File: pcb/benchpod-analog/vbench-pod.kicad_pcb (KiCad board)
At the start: 4 copper layers, 98.9 x 118.2 mm, 236 parts, among them CN1 KH-FPC1.0-H2.0SMT-24P-QCHF, J10 BNC-KYWE-295-W4-N, J11 WJ15EDGRC-3.81-06P, J8 WJ15EDGRC-3.81-02P, J9 WJ15EDGRC-3.81-02P, K1 G6K-2F-Y DC5, K2 G6K-2F-Y DC5, K3 G6K-2F-Y DC5, K4 G6K-2F-Y DC5, Q1 BCP56, U15 TPS7A2045PDBVR, U16 TLV61046ADBVR, U17 TMCP1A106MTRF, U3 TPS7A2050PDQNR, U30 AP2112K-3.3, U36 MCP33131D-10-E/MS, U37 THS4551IRUNR, U38 ADR4540BRZ-R7, U39 AP2112K-1.8TRG1, U40 OPA810IDBVR, U41 LM27761DSGR, U42 LM7705MM/NOPB, U43 DAC8554IPWR, U44 OPA2365AIDR, U45 OPA2992IDR, U46 AP2112K-3.3, U49 TPS65131RGER, U50 TPS7A1901DRBR, U51 OPA2992IDR, U53 TPL7407LAPWR, U58 TCA9554PWR, U61 24C32, U9 XTR116UA/2K5

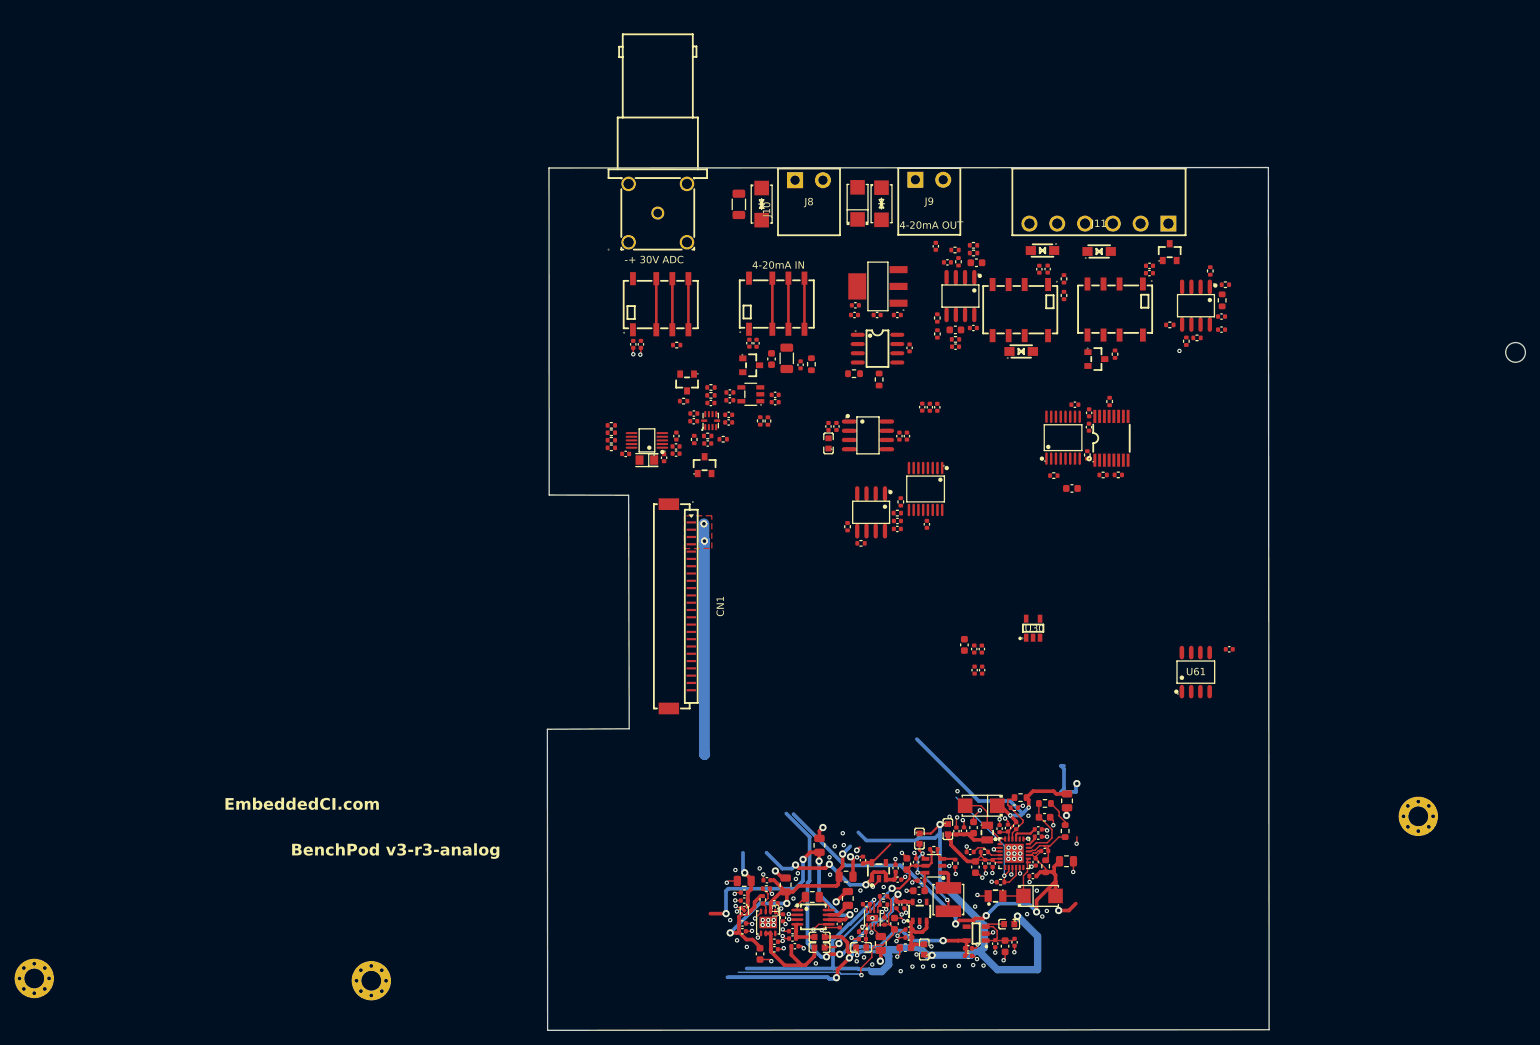
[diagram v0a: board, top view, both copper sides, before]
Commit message: analog only board: square outline, front connectors overhang, J8/J9 turned
Parts moved only; tracks are not rerouted.
- Outline: one polygon, exactly 98.5 x 118 (x 39.0-137.5, y 20.18-138.18),
  with the FFC cut (x to 50.0, y 65.0-97.0) and a 2.2 mm tab under the BNC
  (x 46.41-61.41) so its pads stay on the board while it reaches the panel.
- J10 (ADC BNC): flange front on the panel's inside face (2.4 mm past the
  edge), so the panel nut clamps it; y 26.36 -> 23.78.
- J8 (4-20 IN), J9 (4-20 OUT): were at 0 deg, with the plug opening facing
  into the board; now 180 deg like J11, opening 2.2 mm past the edge.
- J11 (DAC block): 2.2 mm overhang, x 114.37 -> 115.22 for the same
  7.89 mm gap as between J8 and J9.
- J8, J9 and J10 keep their x; nothing else moved.

Co-Authored-By: Claude Opus 5.5 <noreply@anthropic.com>
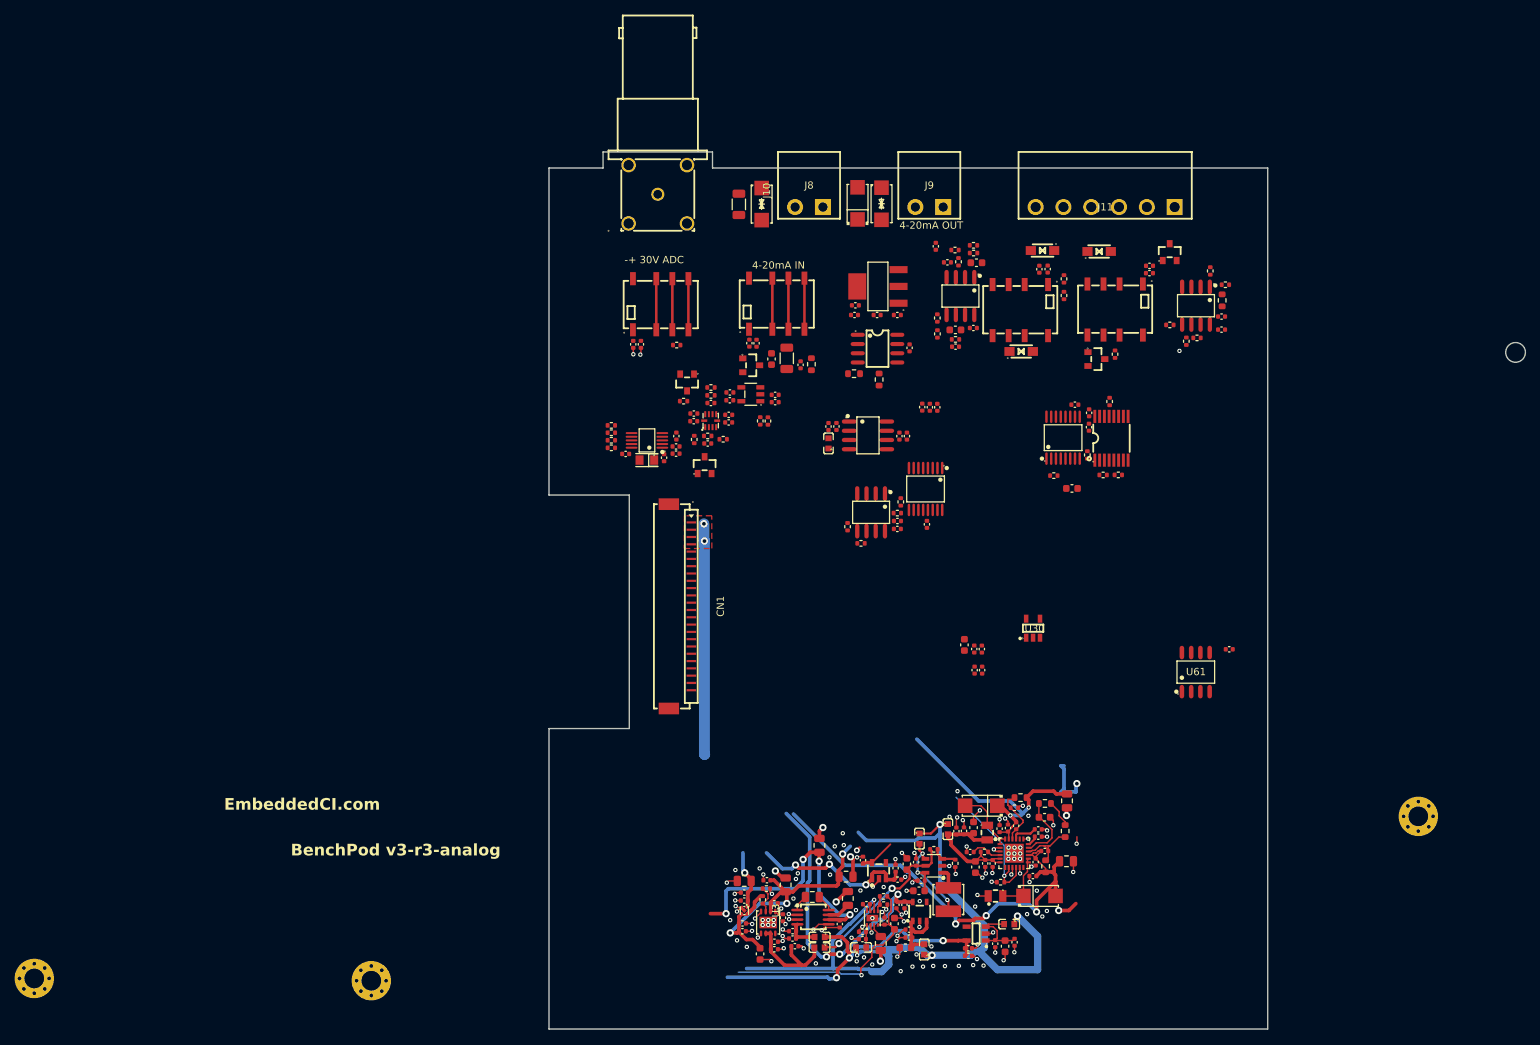
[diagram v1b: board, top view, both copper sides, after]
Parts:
- moved J9 3.74 mm to (91.1, 25.5), turned to 180 degrees
- moved J8 3.68 mm to (74.6, 25.5), turned to 180 degrees
- moved J10 2.58 mm to (53.9, 23.8)
- moved J11 2.42 mm to (115.2, 25.5)
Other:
- board size 98.9 x 118.2 mm -> 98.5 x 120.2 mm

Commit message: analog only board: mounting holes at the digital board's positions
H10, H11, H12, H14 at the same X/Y from the top-left board corner as on the
digital board (x 5.99 / 92.33, y 20.81 / 92.49), so both boards line up
in the case. H10, H11 and H14 sit in free space. H12 lands on U45
(OPA2992), C168, C169 and R108: those need to move. H12 is still the
unplated MountingHole_2.7mm_M2.5 here (plated Pad_Via on the digital
board).

Co-Authored-By: Claude Opus 5.5 <noreply@anthropic.com>
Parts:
- moved H10 95.5 mm to (45.0, 41.0), turned to 0 degrees
- moved H11 78.8 mm to (45.0, 112.7), turned to 0 degrees
- moved H12 40.4 mm to (131.3, 41.0)
- moved H14 27.1 mm to (131.3, 112.7)
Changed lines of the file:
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@@
 	(footprint "MountingHole:MountingHole_2.7mm_M2.5_Pad_Via"
 		(layer "F.Cu")
-		(at 14.65 131.558218 -90)
+		(at 44.992 40.986)
 		(descr "Mounting Hole 2.7mm, M2.5, generated by kicad-footprint-generator mountinghole.py")
 		(tags "mountinghole M2.5")
 		(property "Reference" "H10"
-			(at 0 -3.65 90)
+			(at 0 -3.65 180)
 			(layer "F.SilkS")
 			(hide yes)
@@
 		)
 		(property "Value" "MountingHole"
-			(at 0 3.65 90)
+			(at 0 3.65 180)
 			(layer "F.Fab")
 			(effects
@@
 		)
 		(property "Datasheet" ""
-			(at 0 0 90)
+			(at 0 0 180)
 			(layer "F.Fab")
 			(hide yes)
@@
 		)
 		(property "Description" "Mounting Hole with connection"
-			(at 0 0 90)
+			(at 0 0 180)
 			(layer "F.Fab")
 			(hide yes)
@@
 		)
 		(pad "1" thru_hole circle
-			(at -2.025 0 270)
+			(at -2.025 0)
 			(size 0.8 0.8)
 			(drill 0.5)
@@
 		)
 		(pad "1" thru_hole circle
-			(at -1.431891 -1.431891 270)
+			(at -1.431891 -1.431891)
 			(size 0.8 0.8)
 			(drill 0.5)
@@
 		)
 		(pad "1" thru_hole circle
-			(at -1.431891 1.431891 270)
+			(at -1.431891 1.431891)
 			(size 0.8 0.8)
 			(drill 0.5)
@@
 		)
 		(pad "1" thru_hole circle
-			(at 0 -2.025 270)
+			(at 0 -2.025)
 			(size 0.8 0.8)
 			(drill 0.5)
@@
 		)
 		(pad "1" thru_hole circle
-			(at 0 0 270)
+			(at 0 0)
 			(size 5.4 5.4)
 			(drill 2.7)
@@
 		)
 		(pad "1" thru_hole circle
-			(at 0 2.025 270)
+			(at 0 2.025)
 			(size 0.8 0.8)
 			(drill 0.5)
@@
 		)
 		(pad "1" thru_hole circle
-			(at 1.431891 -1.431891 270)
+			(at 1.431891 -1.431891)
 			(size 0.8 0.8)
 			(drill 0.5)
@@
 		)
 		(pad "1" thru_hole circle
-			(at 1.431891 1.431891 270)
+			(at 1.431891 1.431891)
 			(size 0.8 0.8)
 			(drill 0.5)
@@
 		)
 		(pad "1" thru_hole circle
-			(at 2.025 0 270)
+			(at 2.025 0)
 			(size 0.8 0.8)
 			(drill 0.5)
@@
 	(footprint "MountingHole:MountingHole_2.7mm_M2.5_Pad_Via"
 		(layer "F.Cu")
-		(at -31.538109 131.251109 -90)
+		(at 44.992 112.67)
 		(descr "Mounting Hole 2.7mm, M2.5, generated by kicad-footprint-generator mountinghole.py")
 		(tags "mountinghole M2.5")
 		(property "Reference" "H11"
-			(at 0 -3.65 90)
+			(at 0 -3.65 180)
 			(layer "F.SilkS")
 			(hide yes)
@@
 		)
 		(property "Value" "MountingHole"
-			(at 0 3.65 90)
+			(at 0 3.65 180)
 			(layer "F.Fab")
 			(effects
@@
 		)
 		(property "Datasheet" ""
-			(at 0 0 90)
+			(at 0 0 180)
 			(layer "F.Fab")
 			(hide yes)
@@
 		)
 		(property "Description" "Mounting Hole with connection"
-			(at 0 0 90)
+			(at 0 0 180)
 			(layer "F.Fab")
 			(hide yes)
@@
 		)
 		(pad "1" thru_hole circle
-			(at -2.025 0 270)
+			(at -2.025 0)
 			(size 0.8 0.8)
 			(drill 0.5)
@@
 		)
 		(pad "1" thru_hole circle
-			(at -1.431891 -1.431891 270)
+			(at -1.431891 -1.431891)
 			(size 0.8 0.8)
 			(drill 0.5)
@@
 		)
 		(pad "1" thru_hole circle
-			(at -1.431891 1.431891 270)
+			(at -1.431891 1.431891)
 			(size 0.8 0.8)
 			(drill 0.5)
@@
 		)
 		(pad "1" thru_hole circle
-			(at 0 -2.025 270)
+			(at 0 -2.025)
 			(size 0.8 0.8)
 			(drill 0.5)
@@
 		)
 		(pad "1" thru_hole circle
-			(at 0 0 270)
+			(at 0 0)
 			(size 5.4 5.4)
 			(drill 2.7)
@@
 		)
 		(pad "1" thru_hole circle
-			(at 0 2.025 270)
+			(at 0 2.025)
 			(size 0.8 0.8)
 			(drill 0.5)
@@
 		)
 		(pad "1" thru_hole circle
-			(at 1.431891 -1.431891 270)
+			(at 1.431891 -1.431891)
 			(size 0.8 0.8)
 			(drill 0.5)
@@
 		)
 		(pad "1" thru_hole circle
-			(at 1.431891 1.431891 270)
+			(at 1.431891 1.431891)
 			(size 0.8 0.8)
 			(drill 0.5)
@@
 		)
 		(pad "1" thru_hole circle
-			(at 2.025 0 270)
+			(at 2.025 0)
 			(size 0.8 0.8)
 			(drill 0.5)
@@
 	(footprint "MountingHole:MountingHole_2.7mm_M2.5_Pad_Via"
 		(layer "F.Cu")
-		(at 158.138 109.034)
+		(at 131.332999 112.67)
 		(descr "Mounting Hole 2.7mm, M2.5, generated by kicad-footprint-generator mountinghole.py")
 		(tags "mountinghole M2.5")
@@
 	(footprint "MountingHole:MountingHole_2.7mm_M2.5"
 		(layer "F.Cu")
-		(at 171.463 45.452)
+		(at 131.332999 40.986)
 		(descr "Mounting Hole 2.7mm, M2.5, no annular, generated by kicad-footprint-generator mountinghole.py")
 		(tags "mountinghole M2.5")

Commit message: analog only board: H12 plated and on GND like the other holes
H12 becomes Mechanical:MountingHole_Pad with MountingHole_2.7mm_M2.5_Pad_Via
and its own GND symbol, the same as H10, H11, H14 and all four holes on the
digital board. PCB footprint swapped in place (same position, path, GND on
the pads). Its pad now shorts with U45, C168, C169 and R108, which still
need to move out of the hole's keepout.

Co-Authored-By: Claude Opus 5.5 <noreply@anthropic.com>
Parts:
- H12: footprint MountingHole:MountingHole_2.7mm_M2.5 -> MountingHole:MountingHole_2.7mm_M2.5_Pad_Via
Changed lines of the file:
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@@
 		)
 	)
+	(footprint "MountingHole:MountingHole_2.7mm_M2.5_Pad_Via"
+		(layer "F.Cu")
+		(at 131.332999 40.986)
+		(descr "Mounting Hole 2.7mm, M2.5, generated by kicad-footprint-generator mountinghole.py")
+		(tags "mountinghole M2.5")
+		(property "Reference" "H12"
+			(at 0 -3.65 0)
+			(layer "F.SilkS")
+			(effects
+				(font
+					(size 1 1)
+					(thickness 0.15)
+				)
+			)
+		)
+		(property "Value" "MountingHole"
+			(at 0 3.65 0)
+			(layer "F.Fab")
+			(effects
+				(font
+					(size 1 1)
+					(thickness 0.15)
+				)
+			)
+		)
+		(property "Datasheet" ""
+			(at 0 0 0)
+			(layer "F.Fab")
+			(hide yes)
+			(effects
+				(font
+					(size 1.27 1.27)
+				)
+			)
+		)
+		(property "Description" "Mounting Hole with connection"
+			(at 0 0 0)
+			(layer "F.Fab")
+			(hide yes)
+			(effects
+				(font
+					(size 1.27 1.27)
+				)
+			)
+		)
+		(property "KiLib_Generator" "mounting_hardware/mounting_hole"
+			(at 0 0 0)
+			(layer "F.SilkS")
+			(hide yes)
+			(effects
+				(font
+					(size 1 1)
+					(thickness 0.15)
+				)
+			)
+		)
+		(sheetname "/")
+		(sheetfile "vbench-pod.kicad_sch")
+		(attr exclude_from_pos_files exclude_from_bom)
+		(duplicate_pad_numbers_are_jumpers no)
+		(fp_circle
+			(center 0 0)
+			(end 2.7 0)
+			(stroke
+				(width 0.15)
+				(type solid)
+			)
+			(fill no)
+			(layer "Cmts.User")
+		)
+		(fp_circle
+			(center 0 0)
+			(end 2.95 0)
+			(stroke
+				(width 0.05)
+				(type solid)
+			)
+			(fill no)
+			(layer "F.CrtYd")
+		)
+		(fp_text user "${REFERENCE}"
+			(at 0 0 0)
+			(layer "F.Fab")
+			(effects
+				(font
+					(size 1 1)
+					(thickness 0.15)
+				)
+			)
+		)
+		(pad "1" thru_hole circle
+			(at -2.025 0)
+			(size 0.8 0.8)
+			(drill 0.5)
+			(layers "*.Cu" "*.Mask")
+			(remove_unused_layers no)
+			(net "GND")
+			(zone_connect 2)
+		)
+		(pad "1" thru_hole circle
+			(at -1.431891 -1.431891)
+			(size 0.8 0.8)
+			(drill 0.5)
+			(layers "*.Cu" "*.Mask")
+			(remove_unused_layers no)
+			(net "GND")
+			(zone_connect 2)
+		)
+		(pad "1" thru_hole circle
+			(at -1.431891 1.431891)
+			(size 0.8 0.8)
+			(drill 0.5)
+			(layers "*.Cu" "*.Mask")
+			(remove_unused_layers no)
+			(net "GND")
+			(zone_connect 2)
+		)
+		(pad "1" thru_hole circle
+			(at 0 -2.025)
+			(size 0.8 0.8)
+			(drill 0.5)
+			(layers "*.Cu" "*.Mask")
+			(remove_unused_layers no)
+			(net "GND")
+			(zone_connect 2)
+		)
+		(pad "1" thru_hole circle
+			(at 0 0)
+			(size 5.4 5.4)
+			(drill 2.7)
+			(layers "*.Cu" "*.Mask")
+			(remove_unused_layers no)
+			(net "GND")
+			(zone_connect 2)
+		)
+		(pad "1" thru_hole circle
+			(at 0 2.025)
+			(size 0.8 0.8)
+			(drill 0.5)
+			(layers "*.Cu" "*.Mask")
+			(remove_unused_layers no)
+			(net "GND")
+			(zone_connect 2)
+		)
+		(pad "1" thru_hole circle
+			(at 1.431891 -1.431891)
+			(size 0.8 0.8)
+			(drill 0.5)
+			(layers "*.Cu" "*.Mask")
+			(remove_unused_layers no)
+			(net "GND")
+			(zone_connect 2)
+		)
+		(pad "1" thru_hole circle
+			(at 1.431891 1.431891)
+			(size 0.8 0.8)
+			(drill 0.5)
+			(layers "*.Cu" "*.Mask")
+			(remove_unused_layers no)
+			(net "GND")
+			(zone_connect 2)
+		)
+		(pad "1" thru_hole circle
+			(at 2.025 0)
+			(size 0.8 0.8)
+			(drill 0.5)
+			(layers "*.Cu" "*.Mask")
+			(remove_unused_layers no)
+			(net "GND")
+			(zone_connect 2)
+		)
+		(embedded_fonts no)
+	)
 	(footprint "lcsc:SOIC-8_L5.0-W4.0-P1.27-LS6.0-BL"
 		(layer "F.Cu")
@@
 		)
 	)
-	(footprint "MountingHole:MountingHole_2.7mm_M2.5"
-		(layer "F.Cu")
-		(at 131.332999 40.986)
-		(descr "Mounting Hole 2.7mm, M2.5, no annular, generated by kicad-footprint-generator mountinghole.py")
-		(tags "mountinghole M2.5")
-		(property "Reference" "H12"
-			(at 0 -3.65 0)
-			(layer "F.SilkS")
-			(hide yes)
-			(effects
-				(font
-					(size 1 1)
-					(thickness 0.15)
-				)
-			)
-		)
-		(property "Value" "MountingHole"
-			(at 0 3.65 0)
-			(layer "F.Fab")
-			(effects
-				(font
-					(size 1 1)
-					(thickness 0.15)
-				)
-			)
-		)
-		(property "Datasheet" ""
-			(at 0 0 0)
-			(layer "F.Fab")
-			(hide yes)
-			(effects
-				(font
-					(size 1.27 1.27)
-				)
-			)
-		)
-		(property "Description" "Mounting Hole without connection"
-			(at 0 0 0)
-			(layer "F.Fab")
-			(hide yes)
-			(effects
-				(font
-					(size 1.27 1.27)
-				)
-			)
-		)
-		(property ki_fp_filters "MountingHole*")
-		(sheetname "/")
-		(sheetfile "vbench-pod.kicad_sch")
-		(units
-			(unit
-				(name "A")
-				(pins)
-			)
-		)
-		(attr exclude_from_bom)
-		(duplicate_pad_numbers_are_jumpers no)
-		(fp_circle
-			(center 0 0)
-			(end 2.7 0)
-			(stroke
-				(width 0.15)
-				(type solid)
-			)
-			(fill no)
-			(layer "Cmts.User")
-		)
-		(fp_circle
-			(center 0 0)
-			(end 2.95 0)
-			(stroke
-				(width 0.05)
-				(type solid)
-			)
-			(fill no)
-			(layer "F.CrtYd")
-		)
-		(pad "" np_thru_hole circle
-			(at 0 0)
-			(size 2.7 2.7)
-			(drill 2.7)
-			(layers "*.Cu" "*.Mask")
-		)
-		(embedded_fonts no)
-	)
 	(footprint "lcsc:SOD-123FL_L3.0-W1.8-LS3.7-BI"
